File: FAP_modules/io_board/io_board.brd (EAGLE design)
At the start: 100 x 60 mm, 80 parts, among them IC1 STM32F051C8T6, IC2 EPM240-T100, IC3 24C08BSN, U2 OSCILLATORSMD

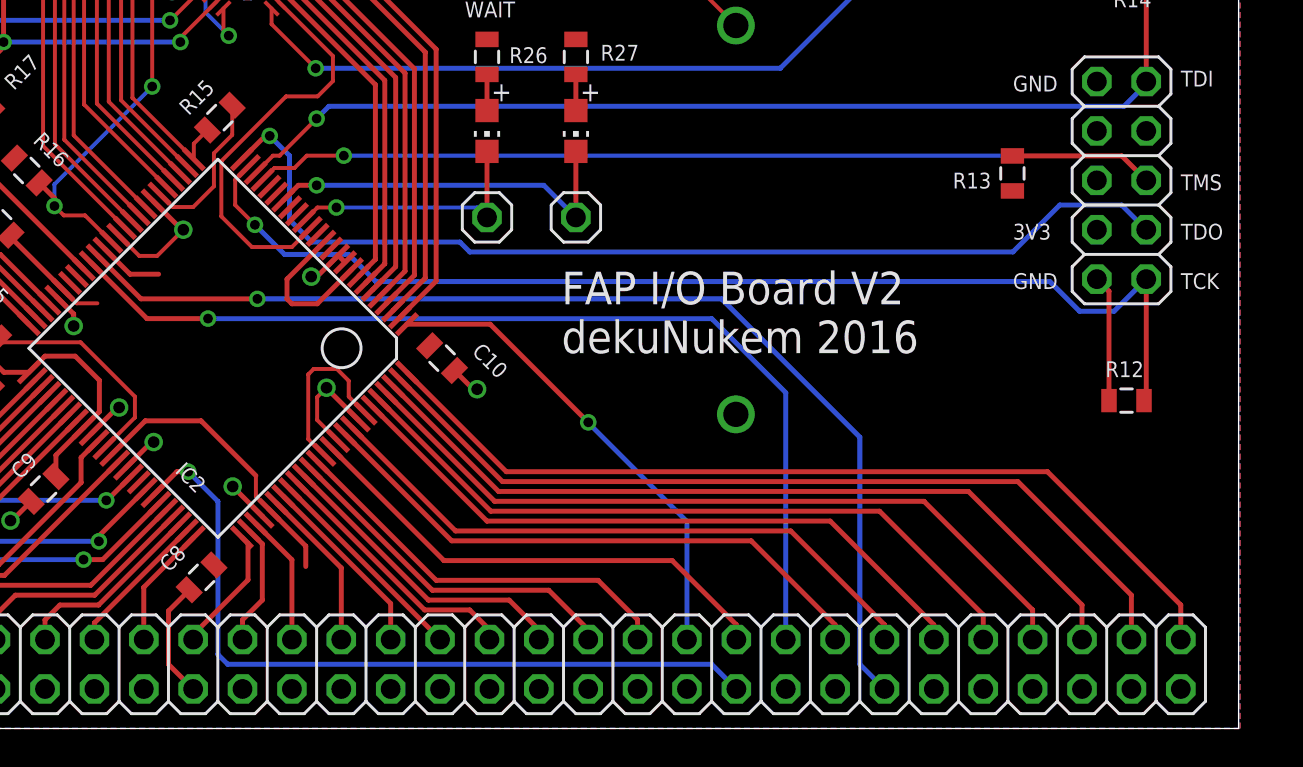
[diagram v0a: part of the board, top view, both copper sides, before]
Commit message: added all Z80 signals on bus
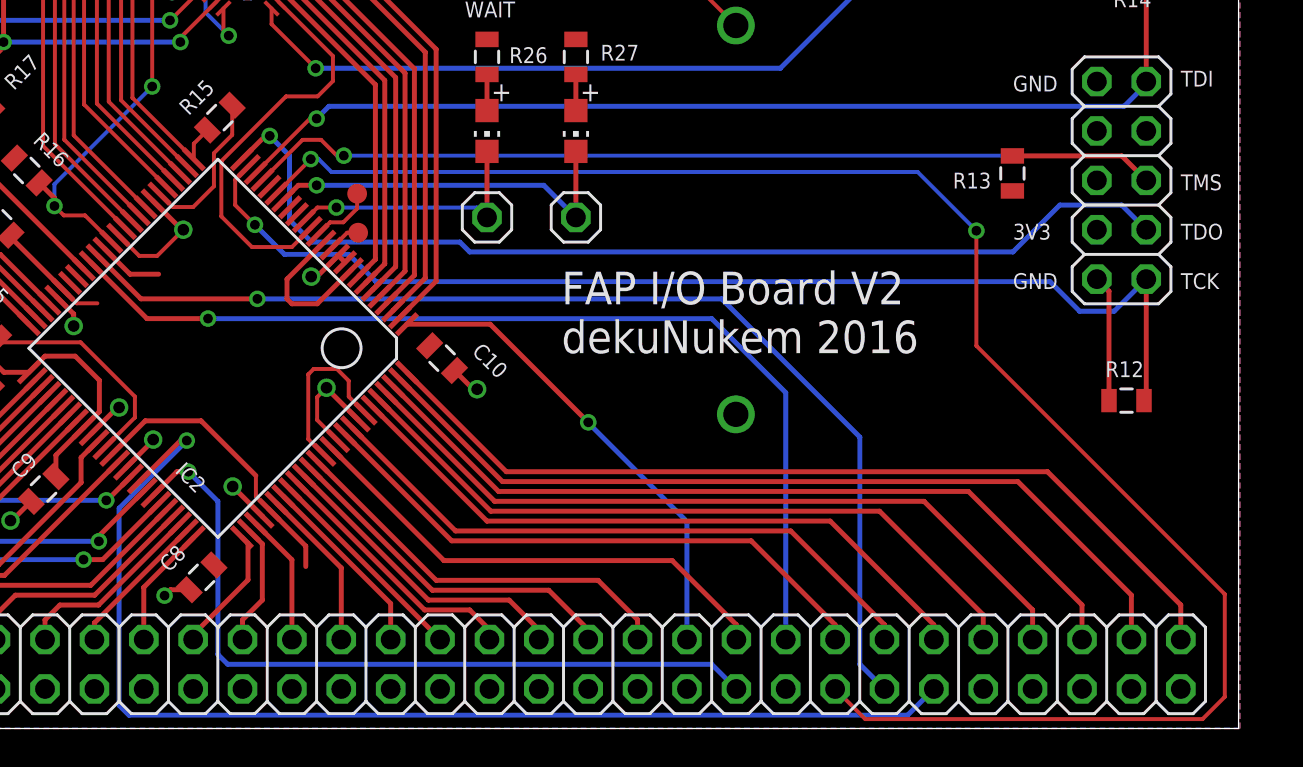
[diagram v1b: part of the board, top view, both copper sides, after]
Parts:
- added TP7, TP8: TEST-POINT3X4, SparkFun-Passives:PAD.03X.04
- U$1: value FAP_BUS_FAP_BUS -> FAP_BUS; device cpu_board:FAP_BUS_2X38 -> fap_bus:2X38
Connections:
- new net N$1: IC2.67, U$1.HALT
- new net N$3: IC2.20, U$1.REFRESH
- new net N$4: IC2.12, TP8.P$1
- new net N$98: IC2.14, TP7.P$1
- net GND: no longer U$1.GND@31, U$1.GND@33
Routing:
- net N$3: track 0.00 -> 88.7 mm, vias 0 -> 2
- net N$1: track 0.00 -> 61.1 mm, vias 0 -> 1
- net GND: track 134.4 -> 129.8 mm, vias 23 -> 24
- net N$98: track 0.00 -> 3.36 mm
- net N$4: track 0.00 -> 1.72 mm
- net TMS: track 53.9 -> 54.6 mm
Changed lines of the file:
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@@
 <setting verticaltext="up"/>
 </settings>
-<grid distance="10" unitdist="mil" unit="mil" style="lines" multiple="1" display="no" altdistance="1" altunitdist="mil" altunit="mil"/>
+<grid distance="1" unitdist="mil" unit="mil" style="lines" multiple="1" display="no" altdistance="1" altunitdist="mil" altunit="mil"/>
 <layers>
 <layer number="1" name="Top" color="4" fill="1" visible="yes" active="yes"/>
@@
 <attribute name="NAME" x="46.971946875" y="12.618896875" size="0.8128" layer="25" ratio="10" rot="R135"/>
 </element>
-<element name="U$1" library="cpu_board" package="FAP_BUS_2X38" value="FAP_BUS_FAP_BUS" x="32.256" y="2.032" smashed="yes"/>
+<element name="U$1" library="fap_bus" package="2X38" value="FAP_BUS" x="32.256" y="2.032" smashed="yes"/>
 <element name="U$2" library="ps2" package="PS/2" value="PS/2" x="2.286" y="22.86" smashed="yes" rot="MR270"/>
 <element name="Y1" library="SparkFun-FreqCtrl" package="HC49US" value="" x="56.1594" y="50.1142" smashed="yes" rot="R315">
@@
 <attribute name="VALUE" x="64.643" y="23.114" size="1.27" layer="27"/>
 </element>
+<element name="TP7" library="SparkFun-Passives" package="PAD.03X.04" value="TEST-POINT3X4" x="54.6608" y="27.5082"/>
+<element name="TP8" library="SparkFun-Passives" package="PAD.03X.04" value="TEST-POINT3X4" x="54.7116" y="25.5016"/>
 </elements>
 <signals>
@@
 <wire x1="53.975" y1="29.464" x2="93.98" y2="29.464" width="0.2032" layer="16"/>
 <wire x1="93.98" y1="29.464" x2="95.25" y2="28.194" width="0.2032" layer="16"/>
-<wire x1="49.796096875" y1="28.22005625" x2="50.405040625" y2="28.829" width="0.2032" layer="1"/>
-<wire x1="50.405040625" y1="28.829" x2="51.435" y2="28.829" width="0.2032" layer="1"/>
-<wire x1="51.435" y1="28.829" x2="52.07" y2="29.464" width="0.2032" layer="1"/>
-<wire x1="52.07" y1="29.464" x2="53.975" y2="29.464" width="0.2032" layer="1"/>
 <wire x1="88.3666" y1="29.4496" x2="93.9944" y2="29.4496" width="0.254" layer="1"/>
 <wire x1="93.9944" y1="29.4496" x2="95.25" y2="28.194" width="0.254" layer="1"/>
+<wire x1="51.852840625" y1="30.2768" x2="52.8066" y2="30.2768" width="0.2032" layer="1"/>
+<wire x1="52.8066" y1="30.2768" x2="53.6194" y2="29.464" width="0.2032" layer="1"/>
+<wire x1="53.6194" y1="29.464" x2="53.975" y2="29.464" width="0.2032" layer="1"/>
+<wire x1="51.852840625" y1="30.2768" x2="49.796096875" y2="28.22005625" width="0.2032" layer="1"/>
 </signal>
 <signal name="TDI">
@@
 <wire x1="94.107" y1="32.004" x2="95.25" y2="33.147" width="0.254" layer="16"/>
 <wire x1="95.25" y1="33.147" x2="95.25" y2="33.274" width="0.254" layer="16"/>
-<wire x1="49.442540625" y1="28.573609375" x2="50.33293125" y2="29.464" width="0.2032" layer="1"/>
-<wire x1="50.33293125" y1="29.464" x2="50.673" y2="29.464" width="0.2032" layer="1"/>
 <wire x1="95.25" y1="33.274" x2="95.25" y2="39.232" width="0.254" layer="1"/>
 <wire x1="95.25" y1="39.232" x2="95.2864" y2="39.2684" width="0.254" layer="1"/>
-<wire x1="50.673" y1="29.464" x2="52.578" y2="31.369" width="0.2032" layer="1"/>
 <wire x1="52.578" y1="31.369" x2="53.213" y2="32.004" width="0.254" layer="16"/>
+<wire x1="49.442540625" y1="28.573609375" x2="52.23793125" y2="31.369" width="0.2032" layer="1"/>
+<wire x1="52.23793125" y1="31.369" x2="52.578" y2="31.369" width="0.2032" layer="1"/>
 </signal>
 <signal name="GND">
@@
 <contactref element="U$1" pad="GND@7"/>
 <contactref element="U$1" pad="GND@18"/>
-<contactref element="U$1" pad="GND@31"/>
 <contactref element="U$1" pad="GND@28"/>
 <contactref element="U$1" pad="GND@34"/>
@@
 <contactref element="U$1" pad="GND@23"/>
 <contactref element="U$1" pad="GND@9"/>
-<contactref element="U$1" pad="GND@33"/>
 <contactref element="JP2" pad="4"/>
 <contactref element="IC2" pad="46"/>
@@
 <via x="52.2986" y="23.241" extent="1-16" drill="0.6"/>
 <via x="40.0812" y="20.701" extent="1-16" drill="0.6"/>
-<via x="44.196" y="14.732" extent="1-16" drill="0.6"/>
+<via x="44.1706" y="14.859" extent="1-16" drill="0.6"/>
 <wire x1="40.957259375" y1="15.13858125" x2="42.328678125" y2="16.51" width="0.254" layer="1"/>
 <wire x1="42.328678125" y1="16.51" x2="42.418" y2="16.51" width="0.254" layer="1"/>
-<wire x1="42.725028125" y1="13.370815625" x2="44.0862125" y2="14.732" width="0.254" layer="1"/>
-<wire x1="44.0862125" y1="14.732" x2="44.196" y2="14.732" width="0.254" layer="1"/>
 <wire x1="53.68518125" y1="24.33096875" x2="53.685184375" y2="24.33096875" width="0.254" layer="1"/>
 <wire x1="53.685184375" y1="24.33096875" x2="54.0387375" y2="23.977415625" width="0.254" layer="1"/>
@@
 <contactref element="C8" pad="1"/>
 <contactref element="C11" pad="1"/>
-<wire x1="46.226" y1="2.032" x2="44.958" y2="3.3" width="0.254" layer="1"/>
-<wire x1="44.958" y1="3.3" x2="44.958" y2="6.0452" width="0.254" layer="1"/>
-<wire x1="44.958" y1="6.0452" x2="46.023403125" y2="7.110603125" width="0.254" layer="1"/>
 <wire x1="46.023403125" y1="7.110603125" x2="46.023403125" y2="7.136003125" width="0.254" layer="1"/>
 <via x="60.833" y="17.4498" extent="1-16" drill="0.6"/>
@@
 <wire x1="93.334" y1="16.8656" x2="93.334" y2="22.49" width="0.254" layer="1"/>
 <wire x1="93.334" y1="22.49" x2="92.71" y2="23.114" width="0.254" layer="1"/>
+<wire x1="42.725028125" y1="13.370815625" x2="44.1706" y2="14.8163875" width="0.254" layer="1"/>
+<wire x1="44.1706" y1="14.8163875" x2="44.1706" y2="14.859" width="0.254" layer="1"/>
+<via x="44.7548" y="6.8326" extent="1-16" drill="0.5"/>
+<wire x1="44.7548" y1="6.8326" x2="45.058203125" y2="7.136003125" width="0.254" layer="1"/>
+<wire x1="45.058203125" y1="7.136003125" x2="46.023403125" y2="7.136003125" width="0.254" layer="1"/>
+<wire x1="41.146" y1="2.032" x2="43.686" y2="2.032" width="0" layer="19" extent="1-1"/>
 </signal>
 <signal name="+3V3">
@@
 <wire x1="59.944" y1="25.019" x2="60.452" y2="24.511" width="0.254" layer="16"/>
 <wire x1="60.452" y1="24.511" x2="88.392" y2="24.511" width="0.254" layer="16"/>
-<wire x1="88.392" y1="24.511" x2="90.805" y2="26.924" width="0.254" layer="16"/>
 <wire x1="90.805" y1="26.924" x2="93.98" y2="26.924" width="0.254" layer="16"/>
 <wire x1="93.98" y1="26.924" x2="95.25" y2="25.654" width="0.254" layer="16"/>
+<wire x1="88.392" y1="24.511" x2="90.805" y2="26.924" width="0.254" layer="16"/>
 </signal>
 <signal name="N$99">
@@
 <wire x1="65.913" y1="29.684" x2="65.913" y2="26.289" width="0.254" layer="1"/>
 </signal>
+<signal name="N$1">
+<contactref element="U$1" pad="HALT"/>
+<contactref element="IC2" pad="67"/>
+<wire x1="84.326" y1="2.032" x2="82.9798" y2="0.6858" width="0.254" layer="16"/>
+<wire x1="82.9798" y1="0.6858" x2="42.926" y2="0.6858" width="0.254" layer="16"/>
+<wire x1="42.926" y1="0.6858" x2="42.418" y2="1.1938" width="0.254" layer="16"/>
+<wire x1="42.418" y1="1.1938" x2="42.418" y2="11.3284" width="0.254" layer="16"/>
+<wire x1="42.418" y1="11.3284" x2="45.8978" y2="14.8082" width="0.254" layer="16"/>
+<via x="45.8978" y="14.8082" extent="1-16" drill="0.5"/>
+<wire x1="45.8978" y1="14.8082" x2="45.576628125" y2="14.8082" width="0.254" layer="1"/>
+<wire x1="45.576628125" y1="14.8082" x2="43.432134375" y2="12.66370625" width="0.254" layer="1"/>
+</signal>
+<signal name="N$3">
+<contactref element="IC2" pad="20"/>
+<contactref element="U$1" pad="REFRESH"/>
+<wire x1="50.503203125" y1="27.51295" x2="52.2732" y2="29.282946875" width="0.2032" layer="1"/>
+<wire x1="52.2732" y1="29.282946875" x2="52.2732" y2="29.2862" width="0.2032" layer="1"/>
+<via x="52.2732" y="29.2862" extent="1-16" drill="0.5"/>
+<wire x1="52.2732" y1="29.2862" x2="52.6796" y2="29.2862" width="0.2032" layer="16"/>
+<wire x1="52.6796" y1="29.2862" x2="53.34" y2="28.6258" width="0.2032" layer="16"/>
+<wire x1="53.34" y1="28.6258" x2="83.4898" y2="28.6258" width="0.2032" layer="16"/>
+<wire x1="83.4898" y1="28.6258" x2="86.5124" y2="25.6032" width="0.2032" layer="16"/>
+<via x="86.5124" y="25.6032" extent="1-16" drill="0.5"/>
+<wire x1="86.5124" y1="25.6032" x2="86.5124" y2="19.685" width="0.2032" layer="1"/>
+<wire x1="86.5124" y1="19.685" x2="99.2886" y2="6.9088" width="0.2032" layer="1"/>
+<wire x1="99.2886" y1="6.9088" x2="99.2886" y2="1.6256" width="0.2032" layer="1"/>
+<wire x1="99.2886" y1="1.6256" x2="98.1456" y2="0.4826" width="0.2032" layer="1"/>
+<wire x1="98.1456" y1="0.4826" x2="80.7954" y2="0.4826" width="0.2032" layer="1"/>
+<wire x1="80.7954" y1="0.4826" x2="79.246" y2="2.032" width="0.2032" layer="1"/>
+</signal>
+<signal name="N$4">
+<contactref element="IC2" pad="12"/>
+<contactref element="TP8" pad="P$1"/>
+<wire x1="53.331628125" y1="24.684521875" x2="54.14870625" y2="25.5016" width="0.2032" layer="1"/>
+<wire x1="54.14870625" y1="25.5016" x2="54.7116" y2="25.5016" width="0.2032" layer="1"/>
+</signal>
+<signal name="N$98">
+<contactref element="IC2" pad="14"/>
+<contactref element="TP7" pad="P$1"/>
+<wire x1="54.6608" y1="27.5082" x2="54.6608" y2="26.7462" width="0.2032" layer="1"/>
+<wire x1="54.6608" y1="26.7462" x2="53.9496" y2="26.035" width="0.2032" layer="1"/>
+<wire x1="53.9496" y1="26.035" x2="53.26789375" y2="26.035" width="0.2032" layer="1"/>
+<wire x1="53.26789375" y1="26.035" x2="52.624521875" y2="25.391628125" width="0.2032" layer="1"/>
+</signal>
 </signals>

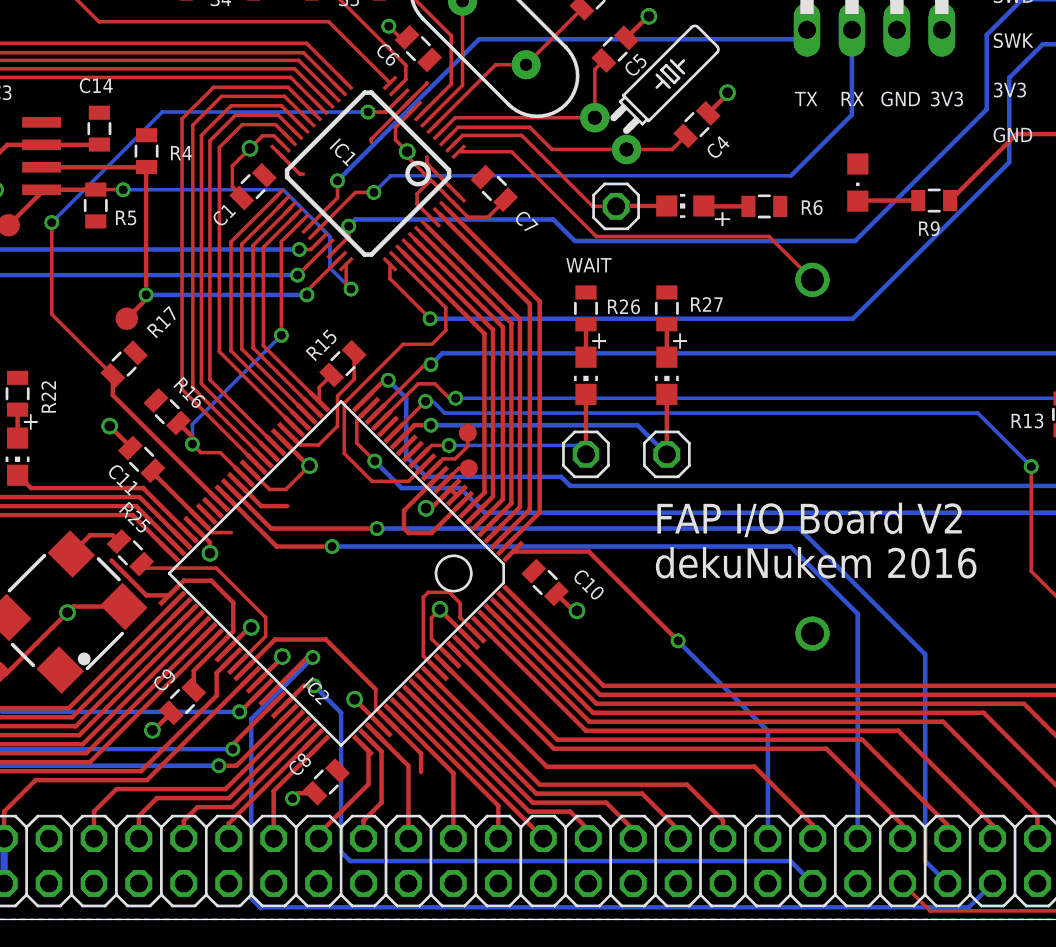
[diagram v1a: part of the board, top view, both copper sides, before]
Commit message: connected BUSREQ to CPLD DEV_OE
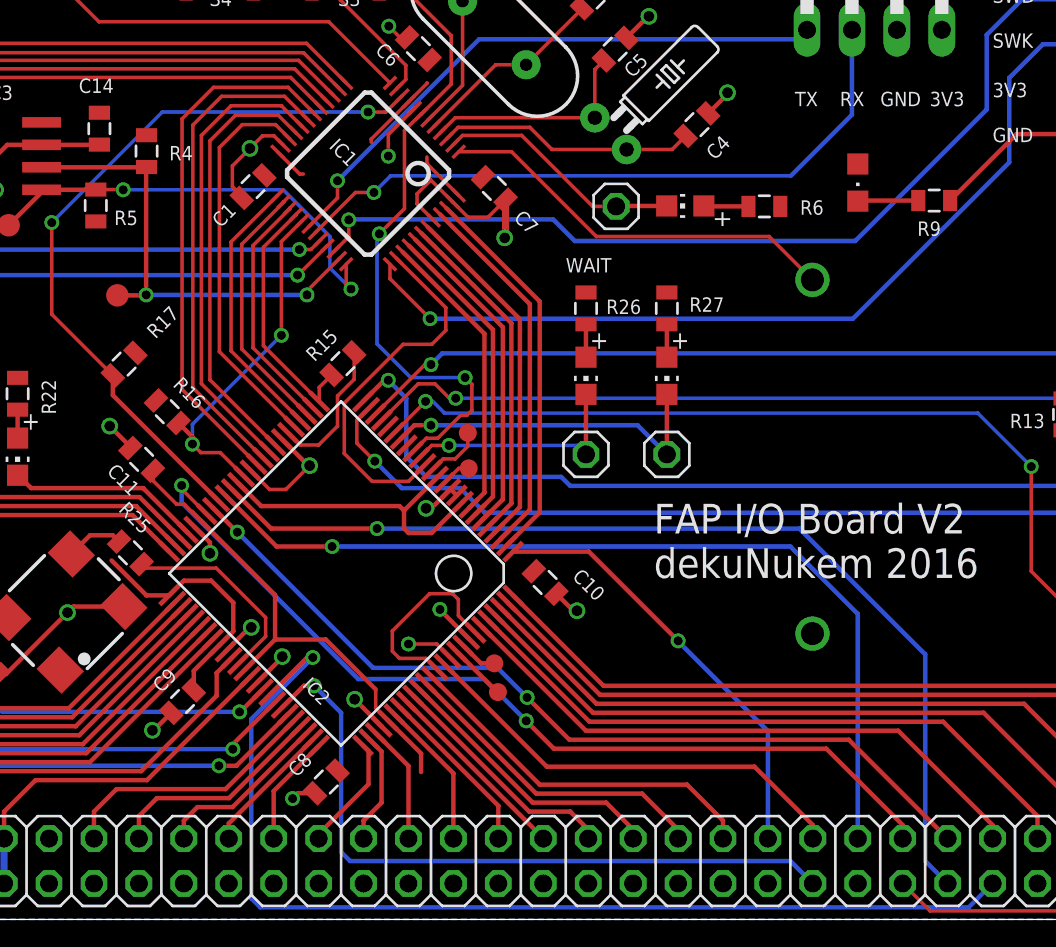
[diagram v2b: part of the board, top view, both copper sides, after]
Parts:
- added TP10, TP9: TEST-POINT3X4, SparkFun-Passives:PAD.03X.04
- moved TP6 1.42 mm to (34.8, 35.3)
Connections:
- new net N$106: IC2.91, TP9.P$1
- new net N$107: IC2.92, TP10.P$1
- net N$14: now also IC2.43; no longer IC2.92
- net N$21: now also IC2.44; no longer IC2.91
- net N$5: now also IC2.17
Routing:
- net N$5: track 15.3 -> 41.4 mm, vias 0 -> 2
- net N$21: track 30.0 -> 52.3 mm, vias 0 -> 2
- net N$14: track 32.4 -> 49.3 mm, vias 0 -> 2
- net +3V3: track 73.7 -> 89.6 mm
- net N$106: track 0.00 -> 3.27 mm
- net N$107: track 0.00 -> 2.19 mm
- net GND: track 129.8 -> 129.4 mm, vias 24 -> 26
